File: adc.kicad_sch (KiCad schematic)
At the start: 26 parts, among them U1 ADA4945-1, U2 LTC2387-18

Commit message: edit README.md
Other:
- company: (none) -> NOIRLab
- title: (none) -> 4 channel ADC Module
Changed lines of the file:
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@@
 	(generator_version "9.0")
 	(paper "A4")
+	(title_block
+		(title "4 channel ADC Module")
+		(date "2025-04-18")
+		(rev "0.1")
+		(company "NOIRLab")
+		(comment 1 "Design: Braulio Cancino Vera - braulio.cancino@noirlab.edu")
+	)
 	(text "Full Power Mode (4mA,  145 MHz), MODE = Vs+\nLow Power Mode (1.4 mA, 80 MHz), MODE = Vs-"
 		(exclude_from_sim no)

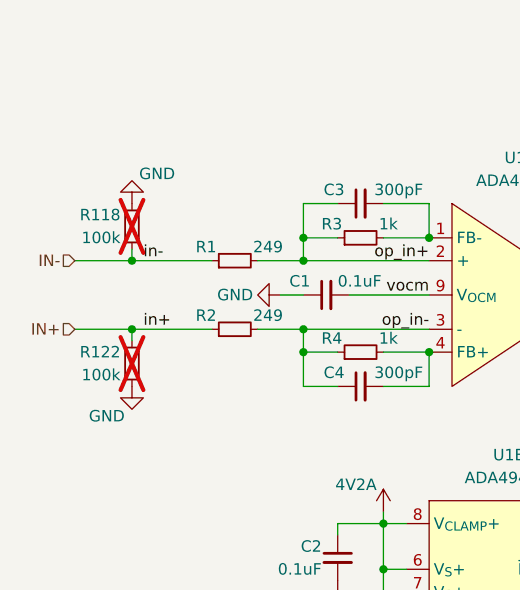
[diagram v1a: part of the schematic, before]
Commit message: Remove floating resistor and reorder schematic pages
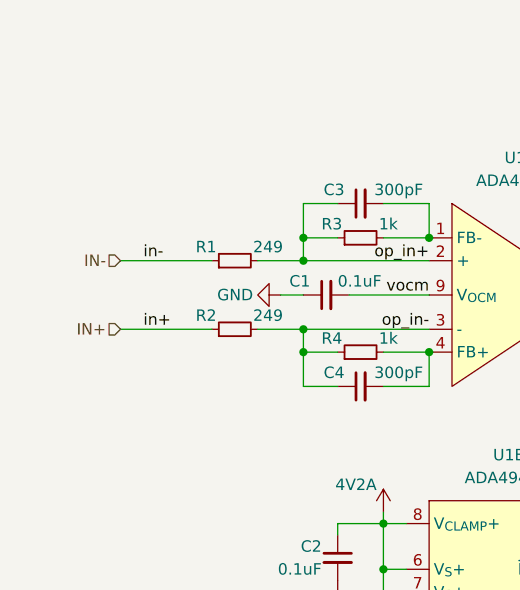
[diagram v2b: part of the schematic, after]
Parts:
- removed R118, R122: 100k, Resistor_SMD:R_0603_1608Metric, symbol Device:R_Small
